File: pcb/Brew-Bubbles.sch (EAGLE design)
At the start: 12 parts, among them U1 GP1A57HR, U2 WEMOS-D1-MINI

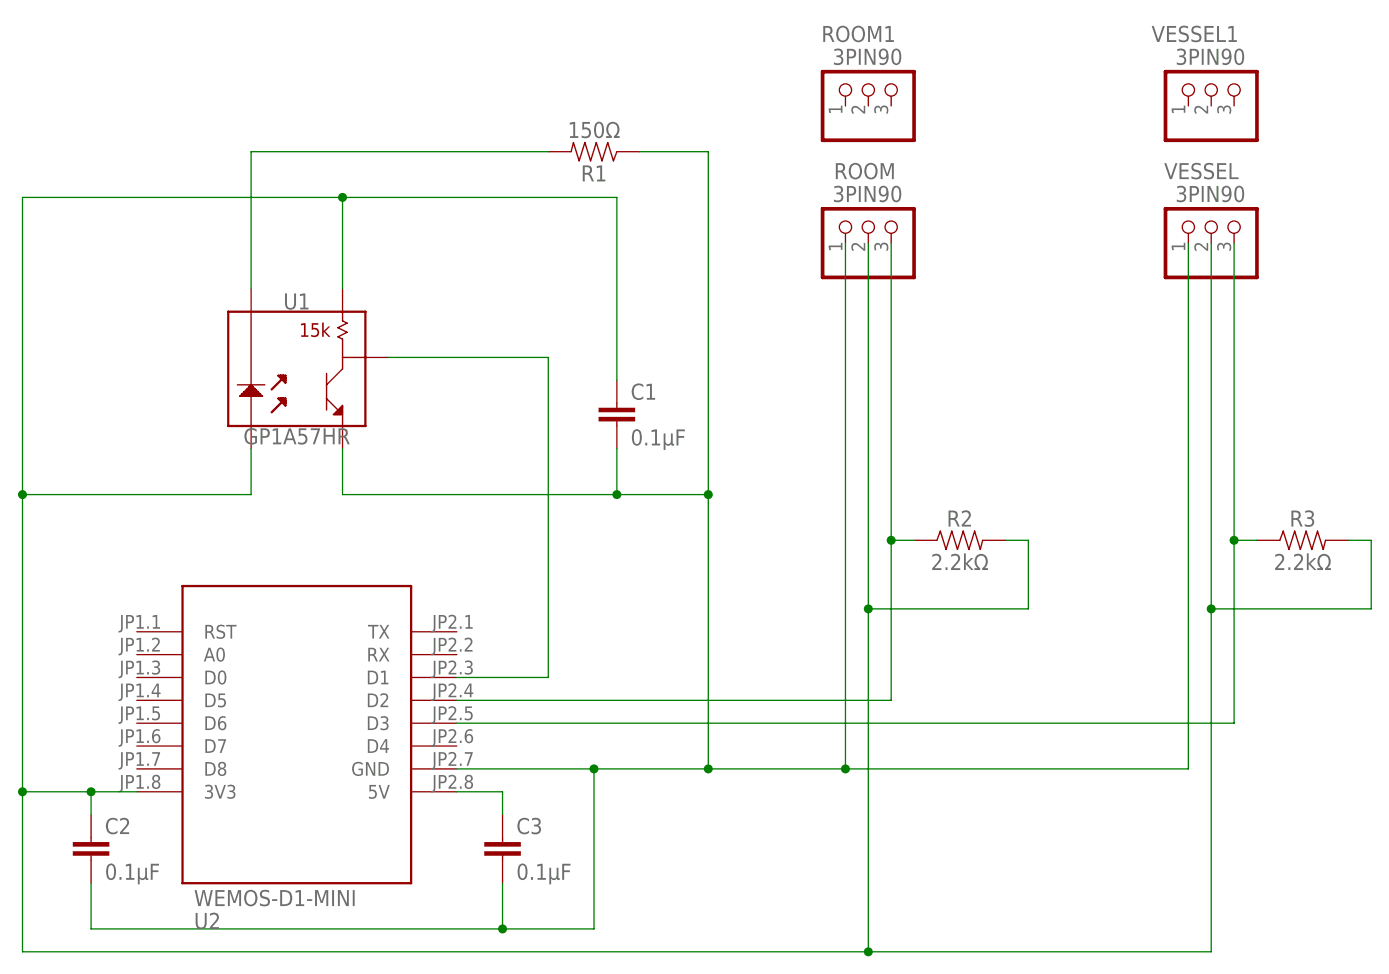
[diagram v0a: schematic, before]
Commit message: Reversed R1 and R3
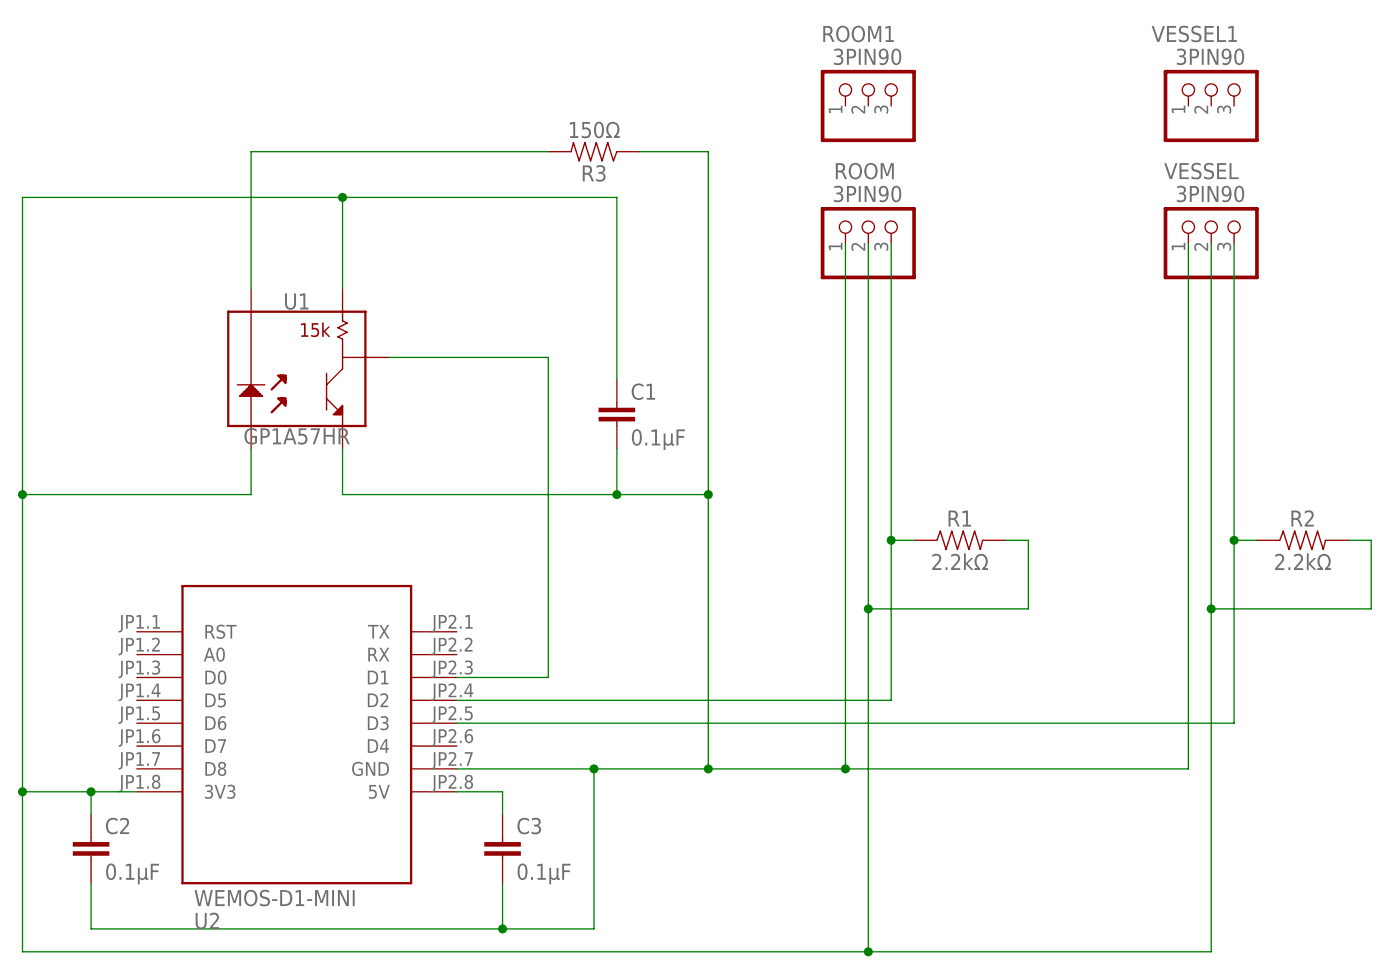
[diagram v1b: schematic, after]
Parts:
- R1: value 150Ω -> 2.2kΩ
- R3: value 2.2kΩ -> 150Ω
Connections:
- net 3V3: now also R1.2; no longer R3.2
- net D2: now also R1.1; no longer R2.1
- net D3: now also R2.1; no longer R3.1
- net GND: now also R3.1; no longer R1.1
- net PD1: now also R3.2; no longer R1.2
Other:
- moved on the sheet: R1, R2, R3
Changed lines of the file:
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@@
 <?xml version="1.0" encoding="utf-8"?>
 <!DOCTYPE eagle SYSTEM "eagle.dtd">
-<eagle version="9.5.0">
+<eagle version="9.4.2">
 <drawing>
 <settings>
@@
 <parts>
 <part name="U2" library="diy-modules" deviceset="WEMOS-D1-MINI-SHIELD" device="" value="WEMOS-D1-MINI"/>
+<part name="R1" library="SparkFun-Resistors" deviceset="330OHM" device="-HORIZ-1/10W-5%" value="2.2kΩ"/>
+<part name="VESSEL" library="pinhead" library_urn="urn:adsk.eagle:library:325" deviceset="PINHD-1X3" device="/90" package3d_urn="urn:adsk.eagle:package:22459/2" value="3PIN90"/>
 <part name="R2" library="SparkFun-Resistors" deviceset="330OHM" device="-HORIZ-1/10W-5%" value="2.2kΩ"/>
-<part name="VESSEL" library="pinhead" library_urn="urn:adsk.eagle:library:325" deviceset="PINHD-1X3" device="/90" package3d_urn="urn:adsk.eagle:package:22459/2" value="3PIN90"/>
-<part name="R3" library="SparkFun-Resistors" deviceset="330OHM" device="-HORIZ-1/10W-5%" value="2.2kΩ"/>
 <part name="U1" library="SparkFun-Sensors" deviceset="GP1A57HR" device=""/>
-<part name="R1" library="SparkFun-Resistors" deviceset="330OHM" device="-HORIZ-1/10W-5%" value="150Ω"/>
+<part name="R3" library="SparkFun-Resistors" deviceset="330OHM" device="-HORIZ-1/10W-5%" value="150Ω"/>
 <part name="ROOM" library="pinhead" library_urn="urn:adsk.eagle:library:325" deviceset="PINHD-1X3" device="/90" package3d_urn="urn:adsk.eagle:package:22459/2" value="3PIN90"/>
 <part name="FRAME1" library="frames" deviceset="LETTER_L" device=""/>
@@
 <attribute name="VALUE" x="6.35" y="33.02" size="1.778" layer="96"/>
 </instance>
-<instance part="R2" gate="G$1" x="91.44" y="73.66" smashed="yes">
+<instance part="R1" gate="G$1" x="91.44" y="73.66" smashed="yes">
 <attribute name="NAME" x="91.44" y="75.184" size="1.778" layer="95" font="vector" align="bottom-center"/>
 <attribute name="VALUE" x="91.44" y="72.136" size="1.778" layer="96" font="vector" align="top-center"/>
@@
 <attribute name="NAME" x="122.428" y="115.57" size="1.778" layer="95" rot="R180"/>
 </instance>
-<instance part="R3" gate="G$1" x="129.54" y="73.66" smashed="yes">
+<instance part="R2" gate="G$1" x="129.54" y="73.66" smashed="yes">
 <attribute name="NAME" x="129.54" y="75.184" size="1.778" layer="95" font="vector" align="bottom-center"/>
 <attribute name="VALUE" x="129.54" y="72.136" size="1.778" layer="96" font="vector" align="top-center"/>
@@
 <attribute name="VALUE" x="17.78" y="86.106" size="1.778" layer="96" font="vector" align="top-center"/>
 </instance>
-<instance part="R1" gate="G$1" x="50.8" y="116.84" smashed="yes" rot="R180">
+<instance part="R3" gate="G$1" x="50.8" y="116.84" smashed="yes" rot="R180">
 <attribute name="NAME" x="50.8" y="115.316" size="1.778" layer="95" font="vector" rot="R180" align="bottom-center"/>
 <attribute name="VALUE" x="50.8" y="118.364" size="1.778" layer="96" font="vector" rot="R180" align="top-center"/>
@@
 <pinref part="U1" gate="G$1" pin="3"/>
 <wire x1="22.86" y1="111.76" x2="22.86" y2="101.6" width="0.1524" layer="91"/>
-<pinref part="R3" gate="G$1" pin="2"/>
 <pinref part="R2" gate="G$1" pin="2"/>
+<pinref part="R1" gate="G$1" pin="2"/>
 <pinref part="VESSEL" gate="A" pin="2"/>
 <pinref part="ROOM" gate="A" pin="2"/>
@@
 <segment>
 <pinref part="U2" gate="G$1" pin="D2"/>
-<pinref part="R2" gate="G$1" pin="1"/>
+<pinref part="R1" gate="G$1" pin="1"/>
 <pinref part="ROOM" gate="A" pin="3"/>
 <wire x1="83.82" y1="55.88" x2="83.82" y2="73.66" width="0.1524" layer="91"/>
@@
 <segment>
 <pinref part="U2" gate="G$1" pin="D3"/>
-<pinref part="R3" gate="G$1" pin="1"/>
+<pinref part="R2" gate="G$1" pin="1"/>
 <pinref part="VESSEL" gate="A" pin="3"/>
 <wire x1="35.56" y1="53.34" x2="121.92" y2="53.34" width="0.1524" layer="91"/>
@@
 <pinref part="U2" gate="G$1" pin="GND"/>
 <pinref part="VESSEL" gate="A" pin="1"/>
-<pinref part="R1" gate="G$1" pin="1"/>
+<pinref part="R3" gate="G$1" pin="1"/>
 <pinref part="U1" gate="G$1" pin="5"/>
 <wire x1="22.86" y1="83.82" x2="22.86" y2="78.74" width="0.1524" layer="91"/>
@@
 <segment>
 <pinref part="U1" gate="G$1" pin="2"/>
-<pinref part="R1" gate="G$1" pin="2"/>
+<pinref part="R3" gate="G$1" pin="2"/>
 <wire x1="45.72" y1="116.84" x2="12.7" y2="116.84" width="0.1524" layer="91"/>
 <wire x1="12.7" y1="116.84" x2="12.7" y2="101.6" width="0.1524" layer="91"/>
